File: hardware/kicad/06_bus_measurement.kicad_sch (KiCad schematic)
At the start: 8 parts, among them U601 INA228 (candidate)

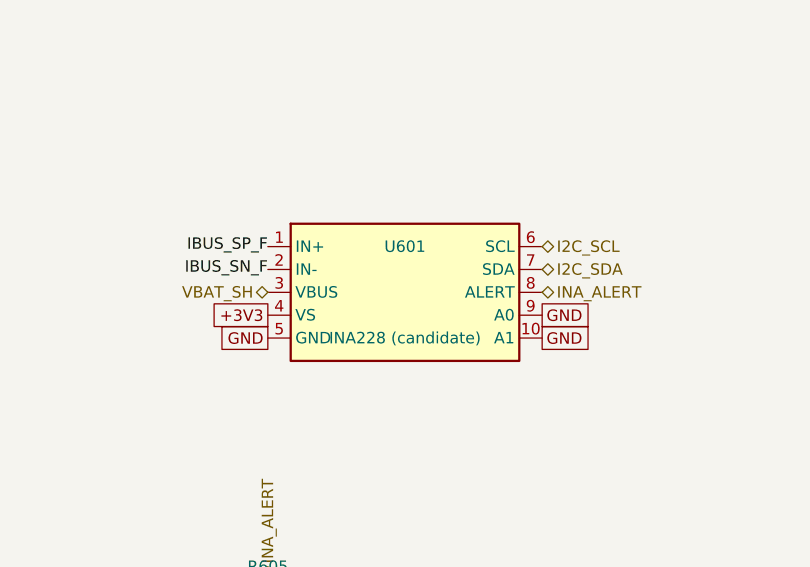
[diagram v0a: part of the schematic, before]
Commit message: sem-motor-controller v0.3: vehicle-interface provenance, transport-neutral core, clock trees, schematic checks
Provenance: the Cornell repositories are reference projects. Every place
that treated CHUDS / CAN FD / its VCU / 40 MHz as our vehicle is relabelled
or corrected (docs/PROVENANCE_AUDIT.md); the v0.2 checkpoint is preserved
with an errata banner.

Firmware: the core is transport-neutral (mc_core_on_msg_rx /
mc_core_msg_tx_poll / mc_core_on_link_state). CAN is one binding
(src/transport/mc_can_binding.c) whose 64-identifier block base is the new
calibration parameter supervision.can_id_base (id 164, rule 40, null in the
unconfigured config). ADR-0012. Tests: block relocation with a full ECO
engagement at 0x500, neutral API, rule-40 C/Python parity.

Clocking: tools/clock_tree.py evaluates 28 complete clock trees x 4 bus
cases from ST register widths and HAL ranges; the v0.2 "40 MHz required"
claim is withdrawn and the crystal is unselected until the bus is known.

Schematic: INA228 pins renumbered (KiCad-library cross-check, secondary);
DRV8353S stays an explicit placeholder; crystal unselected; PWR_FLAGs added
after a new pin-type check (not an ERC) found 6 undriven-rail errors.
Real KiCad ERC not run (KiCad 7 has no CLI ERC; tools/run_kicad_erc.sh).

Telematics: combined architecture with the STM32U575 / CAN 2.0B / LTE-MQTT
proposal (supervisor and CSIA placement, torque-request and driver-
authorization paths, pit/cloud outside the control chain), interface
difference table, generated DBC, logging-capacity and auxiliary-power
budget. Validation language separates command ceilings, envelope ramp,
phase current and battery current. CSIA: component attribution and a
next-evaluation plan; frozen results unchanged, nothing re-run.

Verified on the host: ctest 6/6 (4,006 checks), pytest 199 passed,
ARM core build 0 warnings, generators current, KiCad connectivity 0
problems. Nothing on hardware.

Co-Authored-By: Claude Opus 5.5 <noreply@anthropic.com>
Claude-Ses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
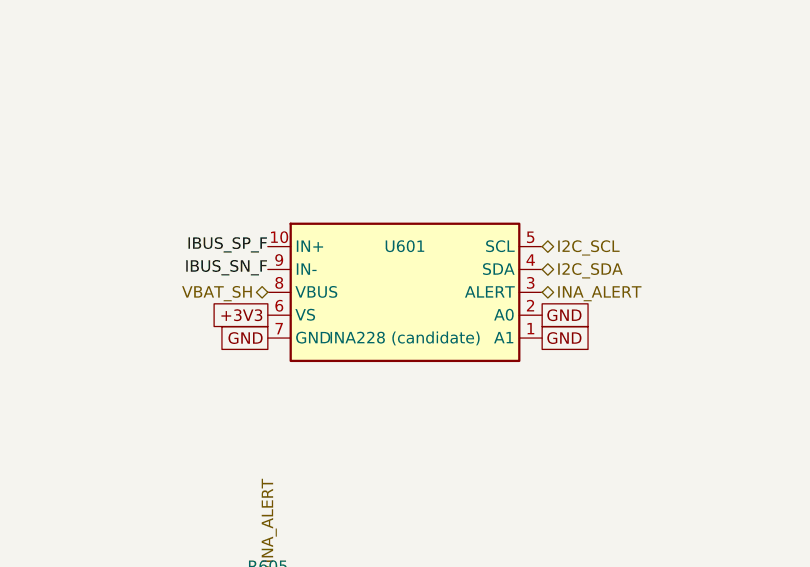
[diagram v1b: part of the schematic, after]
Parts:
- U601: Pin_check UNVERIFIED (pinout not checked against a primary datasheet) -> SECONDARY: numbers match the KiCad official library (INA226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
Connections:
- net +3V3: now also U601.6 (VS); no longer U601.4 (VS)
- net GND: now also U601.1 (A1), U601.2 (A0), U601.7 (GND); no longer U601.10 (A1), U601.5 (GND), U601.9 (A0)
- net I2C_SCL: now also U601.5 (SCL); no longer U601.6 (SCL)
- net I2C_SDA: now also U601.4 (SDA); no longer U601.7 (SDA)
- net IBUS_SN_F: now also U601.9 (IN-); no longer U601.2 (IN-)
- net IBUS_SP_F: now also U601.10 (IN+); no longer U601.1 (IN+)
- net INA_ALERT: now also U601.3 (ALERT); no longer U601.8 (ALERT)
- net VBAT_SH: now also U601.8 (VBUS); no longer U601.3 (VBUS)
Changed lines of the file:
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@@
       (effects (font (size 1.27 1.27)) hide)
     )
-    (property "Pin_check" "UNVERIFIED (pinout not checked against a primary datasheet)" (id 6) (at 86.36 66.04 0)
+    (property "Pin_check" "SECONDARY: numbers match the KiCad official library (INA226-derived VSSOP-10) @cf07d539; primary TI datasheet NOT read" (id 6) (at 86.36 66.04 0)
       (effects (font (size 1.27 1.27)) hide)
     )
-    (pin "1")
-    (pin "2")
-    (pin "3")
-    (pin "4")
-    (pin "5")
+    (pin "10")
+    (pin "9")
+    (pin "8")
     (pin "6")
     (pin "7")
-    (pin "8")
-    (pin "9")
-    (pin "10")
+    (pin "5")
+    (pin "4")
+    (pin "3")
+    (pin "2")
+    (pin "1")
   )
   (symbol (lib_id "Device:R") (at 160.02 66.04 0) (unit 1)

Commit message: hardware: footprint disposition for every BOM line, 82 assigned and checked
hardware/footprints/assignments.yaml gives each of the 122 BOM lines one
disposition. 68 lines are generic parts defined by value and package and
get a verified footprint (37 without the test points); 14 are specific
devices whose footprint is assigned from the KiCad 8.0.9 library but whose
manufacturer package drawing is unread (the LM5164 land pattern is drawn
from ST's L5973D HSOP-8 and the LQFP-100 from NXP's SOT407-1, so both must
be compared); 40 have none and say why: 28 rating-dependent, 4 waiting for a
data sheet value or pin voltage, 6 connectors, 2 placeholder pinouts.
Before this change no line had a footprint.

tools/check_footprints.py fetches the 25 footprint files used, pins them by
SHA-256, and checks per reference: numbered pads equal the symbol's pin
numbers, courtyard and fabrication outline present (copper-only jumpers and
net ties excepted), SMD or through-hole, package in the name for chip
parts, the symbol's footprint filters (as KiCad's ERC does), and pin 1 = K
on diode and LED symbols. Mutation tests cover a wrong pad count, a filter
miss, a package mismatch, a missing reference and a verified line without
a footprint. Small passives on battery-voltage nets (R104, R201, R202,
R1201) were kept rating-dependent rather than given an 0603.

The generator writes the footprints into the schematic and a footprint
column into the draft BOM; hw_consistency adds BM3 (netlist footprint
equals the BOM line's); price_bom takes footprint and package from the
assignment. Pricing rules fixed where lines matched the wrong rule: LEDs
were priced as buck inductors, crystal load capacitors as 100 V MLCCs, the
UART bench header as a harness connector, the reset switch and the Zener
under one generic rule; 22 uF and 4.7 uF now 1206 and 0805 for DC bias. One
board's parts move from $89-$239 to $88-$233. A project fp-lib-table and
the CI and ERC steps fetch the pinned footprints so the ERC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
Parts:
- C601, C602: footprint (none) -> Capacitor_SMD:C_0603_1608Metric
- R601, R602, R603, R604, R605: footprint (none) -> Resistor_SMD:R_0603_1608Metric
- U601: footprint (none) -> Package_SO:VSSOP-10_3x3mm_P0.5mm
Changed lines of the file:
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@@
       (effects (font (size 1.27 1.27)))
     )
-    (property "Footprint" "" (id 2) (at 86.36 66.04 0)
+    (property "Footprint" "Package_SO:VSSOP-10_3x3mm_P0.5mm" (id 2) (at 86.36 66.04 0)
       (effects (font (size 1.27 1.27)) hide)
     )
@@
       (effects (font (size 1.27 1.27)))
     )
-    (property "Footprint" "" (id 2) (at 160.02 66.04 0)
+    (property "Footprint" "Resistor_SMD:R_0603_1608Metric" (id 2) (at 160.02 66.04 0)
       (effects (font (size 1.27 1.27)) hide)
     )
@@
       (effects (font (size 1.27 1.27)))
     )
-    (property "Footprint" "" (id 2) (at 220.98 66.04 0)
+    (property "Footprint" "Resistor_SMD:R_0603_1608Metric" (id 2) (at 220.98 66.04 0)
       (effects (font (size 1.27 1.27)) hide)
     )
@@
       (effects (font (size 1.27 1.27)))
     )
-    (property "Footprint" "" (id 2) (at 279.4 66.04 0)
+    (property "Footprint" "Capacitor_SMD:C_0603_1608Metric" (id 2) (at 279.4 66.04 0)
       (effects (font (size 1.27 1.27)) hide)
     )
@@
       (effects (font (size 1.27 1.27)))
     )
-    (property "Footprint" "" (id 2) (at 340.36 66.04 0)
+    (property "Footprint" "Capacitor_SMD:C_0603_1608Metric" (id 2) (at 340.36 66.04 0)
       (effects (font (size 1.27 1.27)) hide)
     )
@@
       (effects (font (size 1.27 1.27)))
     )
-    (property "Footprint" "" (id 2) (at 401.32 66.04 0)
+    (property "Footprint" "Resistor_SMD:R_0603_1608Metric" (id 2) (at 401.32 66.04 0)
       (effects (font (size 1.27 1.27)) hide)
     )
@@
       (effects (font (size 1.27 1.27)))
     )
-    (property "Footprint" "" (id 2) (at 459.74 66.04 0)
+    (property "Footprint" "Resistor_SMD:R_0603_1608Metric" (id 2) (at 459.74 66.04 0)
       (effects (font (size 1.27 1.27)) hide)
     )
@@
       (effects (font (size 1.27 1.27)))
     )
-    (property "Footprint" "" (id 2) (at 71.12 101.6 0)
+    (property "Footprint" "Resistor_SMD:R_0603_1608Metric" (id 2) (at 71.12 101.6 0)
       (effects (font (size 1.27 1.27)) hide)
     )
